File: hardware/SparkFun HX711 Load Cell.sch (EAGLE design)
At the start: 25 parts, among them Q1 MMBT4403, U1 HX711, U7 OSHW-LOGOS

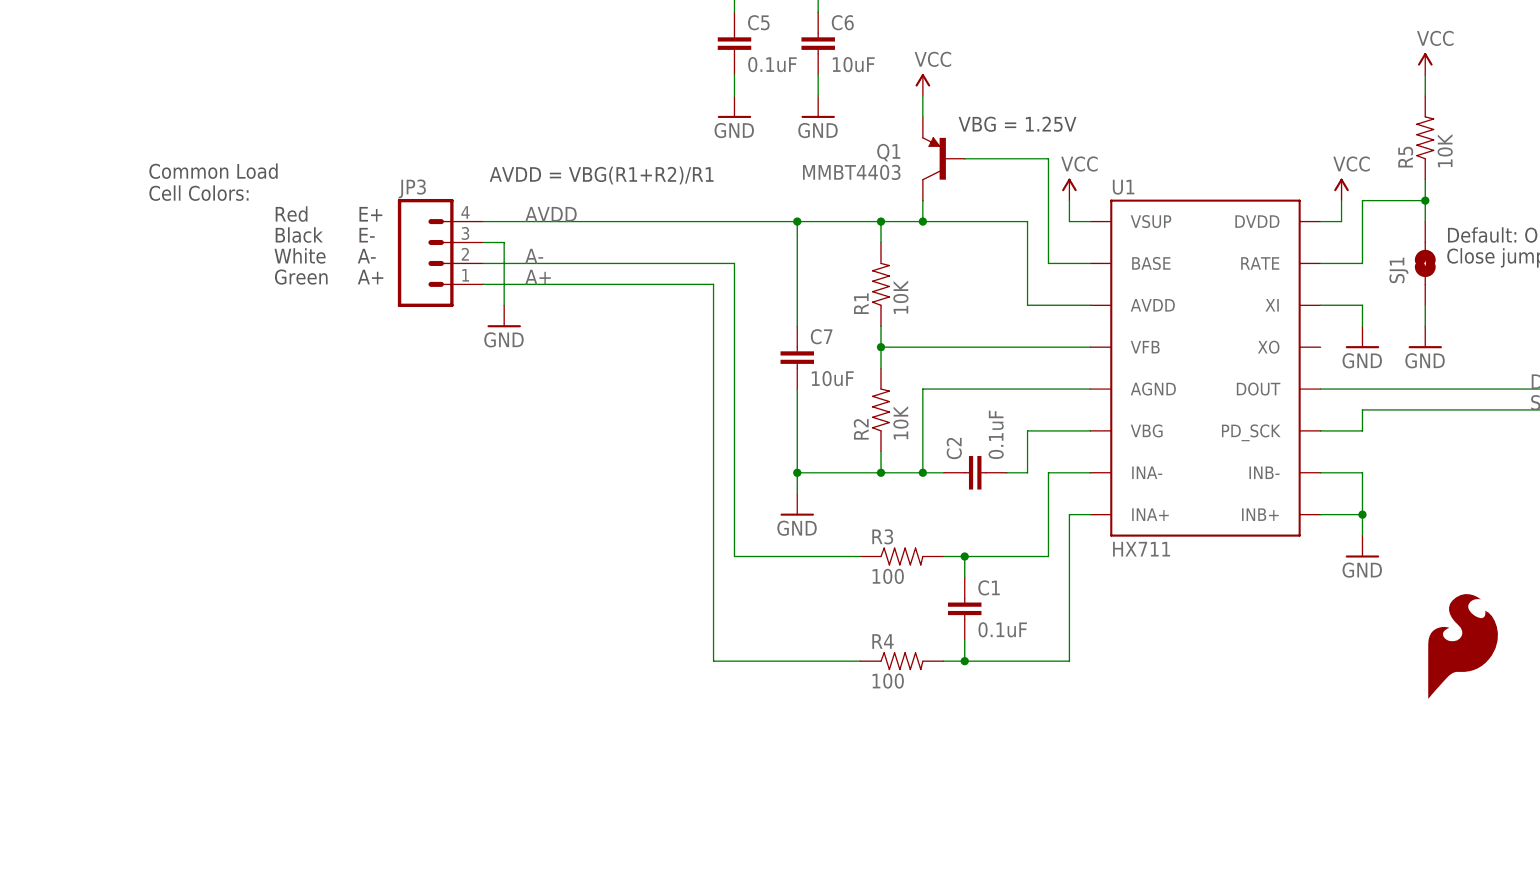
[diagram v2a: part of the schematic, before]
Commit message: Broke out channel B. Adjusted some traces.
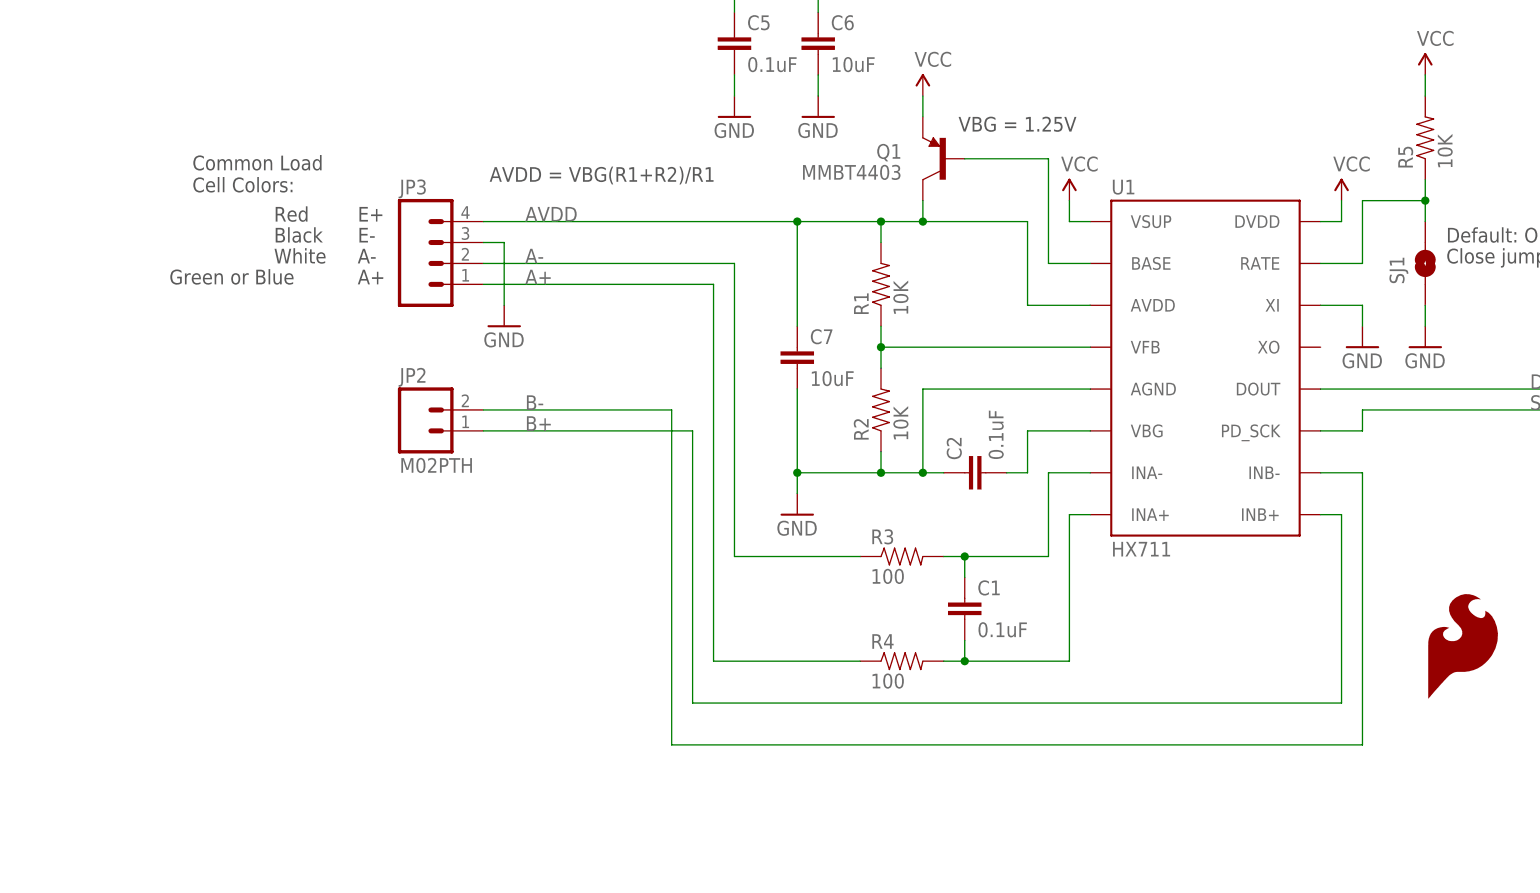
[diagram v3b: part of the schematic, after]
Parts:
- added JP2: M02PTH, SparkFun-Connectors:M02PTH
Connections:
- new net B+: JP2.1, U1.INB+
- new net B-: JP2.2, U1.INB-
- net GND: no longer U1.INB+, U1.INB-
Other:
- note added: "Green or Blue"
- note removed: "Green"
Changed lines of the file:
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@@
 <?xml version="1.0" encoding="utf-8"?>
 <!DOCTYPE eagle SYSTEM "eagle.dtd">
-<eagle version="6.5.0">
+<eagle version="7.1.0">
 <drawing>
 <settings>
@@
 <layer number="56" name="wert" color="7" fill="1" visible="no" active="no"/>
 <layer number="57" name="tCAD" color="7" fill="1" visible="no" active="no"/>
+<layer number="90" name="Modules" color="5" fill="1" visible="yes" active="yes"/>
 <layer number="91" name="Nets" color="2" fill="1" visible="yes" active="yes"/>
 <layer number="92" name="Busses" color="1" fill="1" visible="yes" active="yes"/>
@@
 <part name="GND5" library="SparkFun-Aesthetics" deviceset="GND" device=""/>
 <part name="JP3" library="SparkFun-Connectors" deviceset="M04" device="PTH"/>
-<part name="GND6" library="SparkFun-Aesthetics" deviceset="GND" device=""/>
 <part name="SUPPLY5" library="SparkFun-Aesthetics" deviceset="VCC" device=""/>
 <part name="R5" library="SparkFun-Resistors" deviceset="10KOHM1/10W1%(0603)" device="0603" value="10K"/>
@@
 <part name="FID1" library="SparkFun-Aesthetics" deviceset="FIDUCIAL" device="1X2"/>
 <part name="FID2" library="SparkFun-Aesthetics" deviceset="FIDUCIAL" device="1X2"/>
+<part name="JP2" library="SparkFun-Connectors" deviceset="M02" device="PTH"/>
 </parts>
 <sheets>
@@
 <text x="38.1" y="121.92" size="1.778" layer="97">Black</text>
 <text x="38.1" y="119.38" size="1.778" layer="97">White</text>
-<text x="38.1" y="116.84" size="1.778" layer="97">Green</text>
-<text x="22.86" y="127" size="1.778" layer="97">Common Load
+<text x="25.4" y="116.84" size="1.778" layer="97">Green or Blue</text>
+<text x="28.194" y="128.016" size="1.778" layer="97">Common Load
 Cell Colors:</text>
 <text x="172.72" y="10.16" size="1.778" layer="94">N. Seidle</text>
@@
 <instance part="GND5" gate="1" x="101.6" y="88.9"/>
 <instance part="JP3" gate="G$1" x="58.42" y="119.38"/>
-<instance part="GND6" gate="1" x="170.18" y="83.82"/>
 <instance part="SUPPLY5" gate="G$1" x="195.58" y="109.22"/>
 <instance part="R5" gate="G$1" x="177.8" y="134.62" rot="R90"/>
@@
 <instance part="FID1" gate="G$1" x="243.84" y="43.18"/>
 <instance part="FID2" gate="G$1" x="238.76" y="43.18"/>
+<instance part="JP2" gate="G$1" x="55.88" y="99.06"/>
 </instances>
 <busses>
@@
 <junction x="101.6" y="93.98"/>
 <pinref part="C2" gate="G$1" pin="1"/>
-</segment>
-<segment>
-<pinref part="U1" gate="U1" pin="INB-"/>
-<pinref part="GND6" gate="1" pin="GND"/>
-<wire x1="165.1" y1="93.98" x2="170.18" y2="93.98" width="0.1524" layer="91"/>
-<wire x1="170.18" y1="93.98" x2="170.18" y2="88.9" width="0.1524" layer="91"/>
-<pinref part="U1" gate="U1" pin="INB+"/>
-<wire x1="170.18" y1="88.9" x2="170.18" y2="86.36" width="0.1524" layer="91"/>
-<wire x1="165.1" y1="88.9" x2="170.18" y2="88.9" width="0.1524" layer="91"/>
-<junction x="170.18" y="88.9"/>
 </segment>
 <segment>
@@
 </segment>
 </net>
+<net name="B+" class="0">
+<segment>
+<pinref part="U1" gate="U1" pin="INB+"/>
+<wire x1="165.1" y1="88.9" x2="167.64" y2="88.9" width="0.1524" layer="91"/>
+<wire x1="167.64" y1="88.9" x2="167.64" y2="66.04" width="0.1524" layer="91"/>
+<wire x1="167.64" y1="66.04" x2="88.9" y2="66.04" width="0.1524" layer="91"/>
+<wire x1="88.9" y1="66.04" x2="88.9" y2="99.06" width="0.1524" layer="91"/>
+<pinref part="JP2" gate="G$1" pin="1"/>
+<wire x1="88.9" y1="99.06" x2="63.5" y2="99.06" width="0.1524" layer="91"/>
+<label x="68.58" y="99.06" size="1.778" layer="95"/>
+</segment>
+</net>
+<net name="B-" class="0">
+<segment>
+<pinref part="U1" gate="U1" pin="INB-"/>
+<wire x1="165.1" y1="93.98" x2="170.18" y2="93.98" width="0.1524" layer="91"/>
+<wire x1="170.18" y1="93.98" x2="170.18" y2="60.96" width="0.1524" layer="91"/>
+<wire x1="170.18" y1="60.96" x2="86.36" y2="60.96" width="0.1524" layer="91"/>
+<wire x1="86.36" y1="60.96" x2="86.36" y2="101.6" width="0.1524" layer="91"/>
+<pinref part="JP2" gate="G$1" pin="2"/>
+<wire x1="86.36" y1="101.6" x2="63.5" y2="101.6" width="0.1524" layer="91"/>
+<label x="68.58" y="101.6" size="1.778" layer="95"/>
+</segment>
+</net>

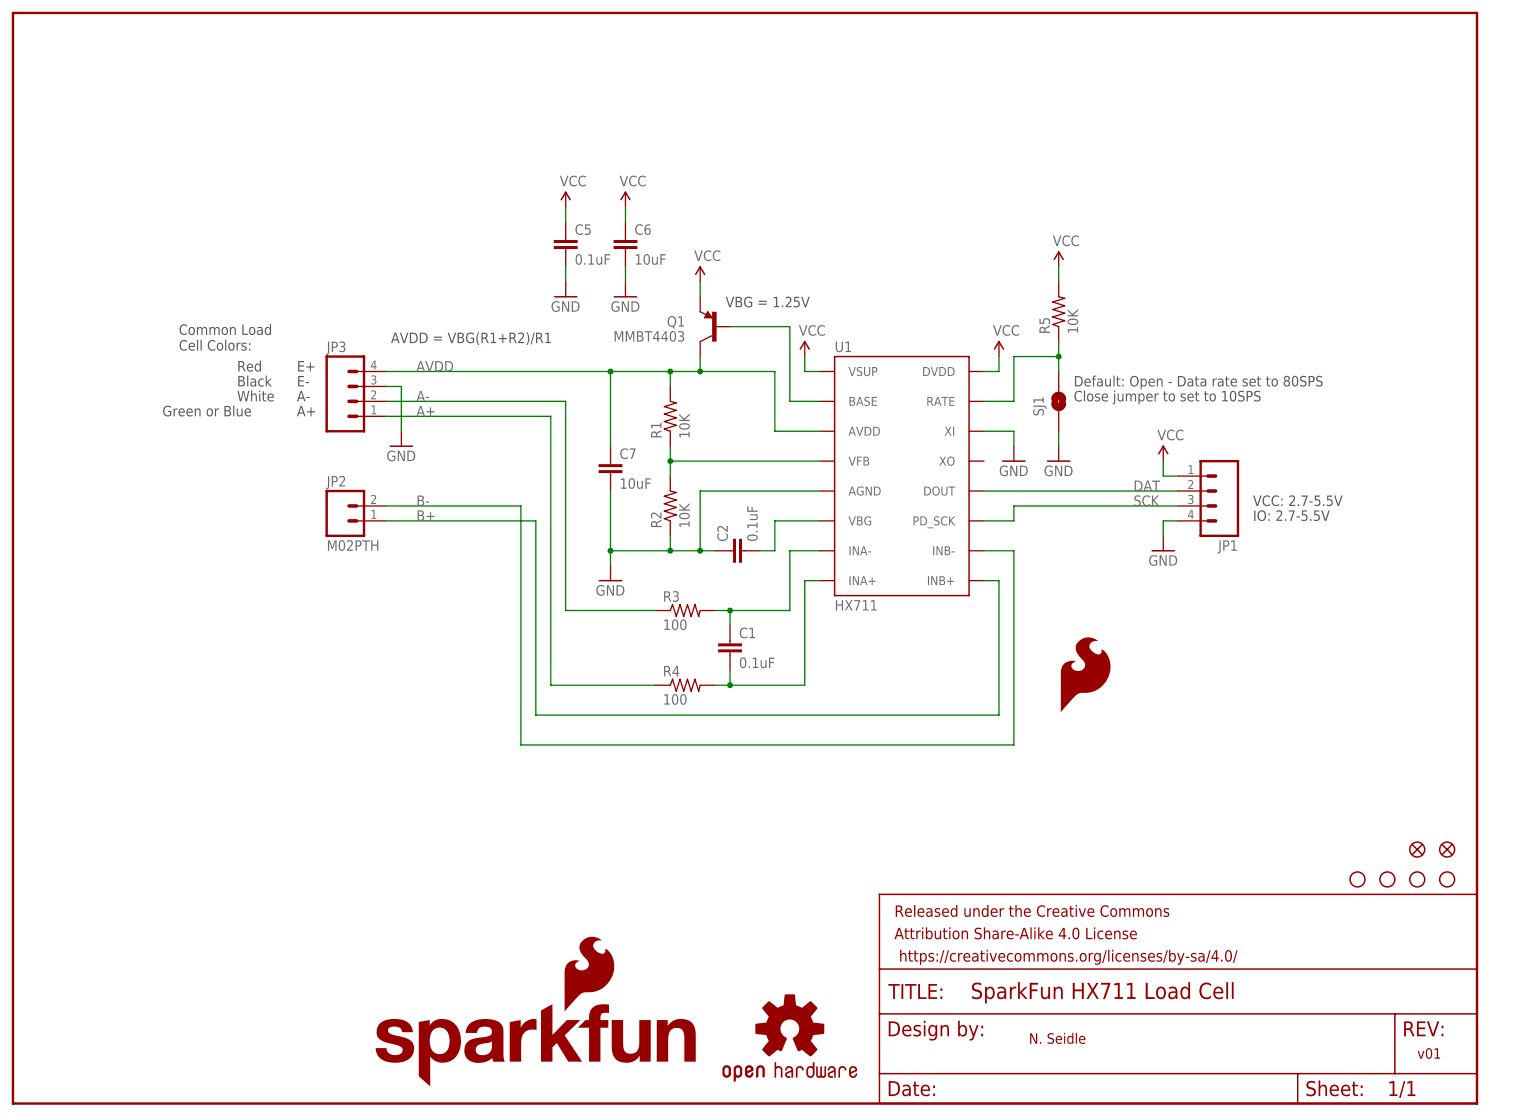
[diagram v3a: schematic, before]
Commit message: Silk label adjustment. Added cnt for shielding (yellow).
Some load cells have a 5th wire that is yellow that shields the four
wires. Added a ground connection for this 5th wire.
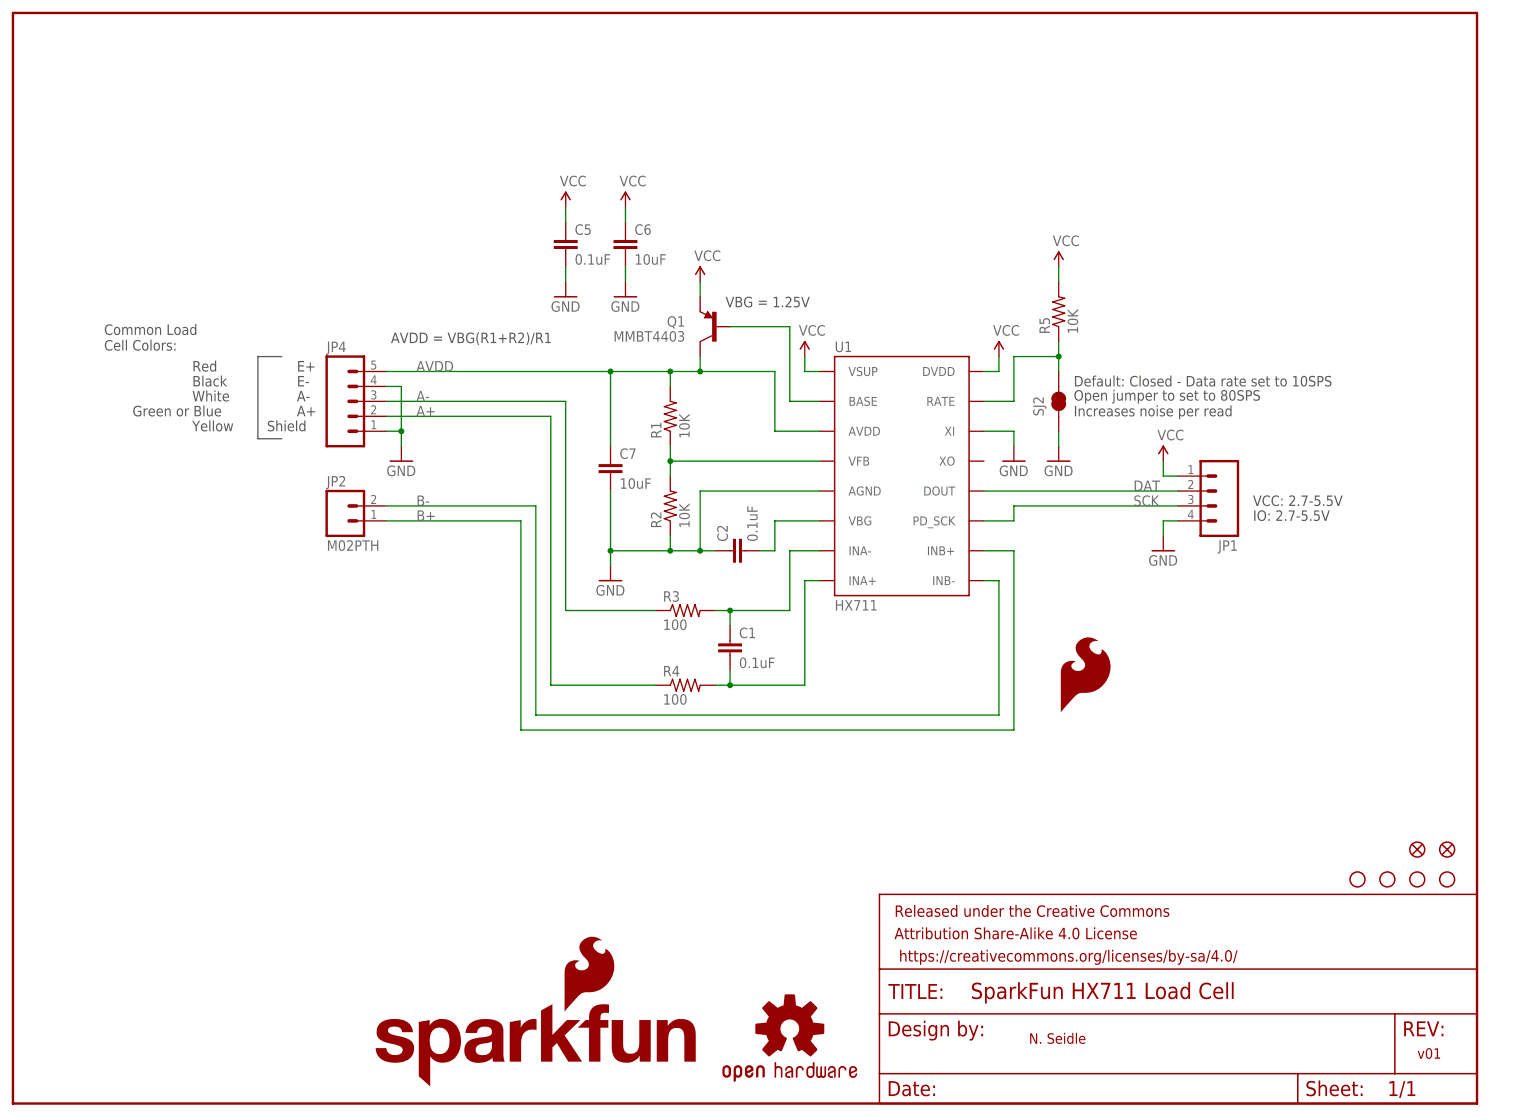
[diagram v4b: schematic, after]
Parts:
- removed JP3: (no value), SparkFun-Connectors:M04PTH
- removed SJ1: JUMPER-PAD-2-NOYES_SILK, SparkFun-Passives:JUMPER-PAD-2-NOYES_SILK
- added JP4: (no value), SparkFun-Connectors:M05PTH
- added SJ2: JUMPER-PAD-2-NC_BY_TRACE, SparkFun-Passives:JUMPER-PAD-2-NC_BY_TRACE
- R1, R2, R5: device SparkFun-Resistors:10KOHM1/10W1%(0603)0603 -> SparkFun-Resistors:10KOHM-1/10W-1%(0603)0603
- R3, R4: device SparkFun-Resistors:100OHM1/10W1%(0603) -> SparkFun-Resistors:100OHM-1/10W-1%(0603)
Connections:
- net A+: now also JP4.2; no longer JP3.1
- net A-: now also JP4.3; no longer JP3.2
- net AVDD: now also JP4.5; no longer JP3.4
- net GND: now also JP4.1, JP4.4, SJ2.1; no longer JP3.3, SJ1.1
- net N$1: now also SJ2.2; no longer SJ1.2
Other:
- note added: "Default: Closed - Data rate set to 10SPS"
- note added: "Open jumper to set to 80SPS Increases noise per read"
- note added: "Shield"
- note added: "Yellow"
- note removed: "Close jumper to set to 10SPS"
- note removed: "Default: Open - Data rate set to 80SPS"

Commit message: Change AVDD resistors to output closer to 5V
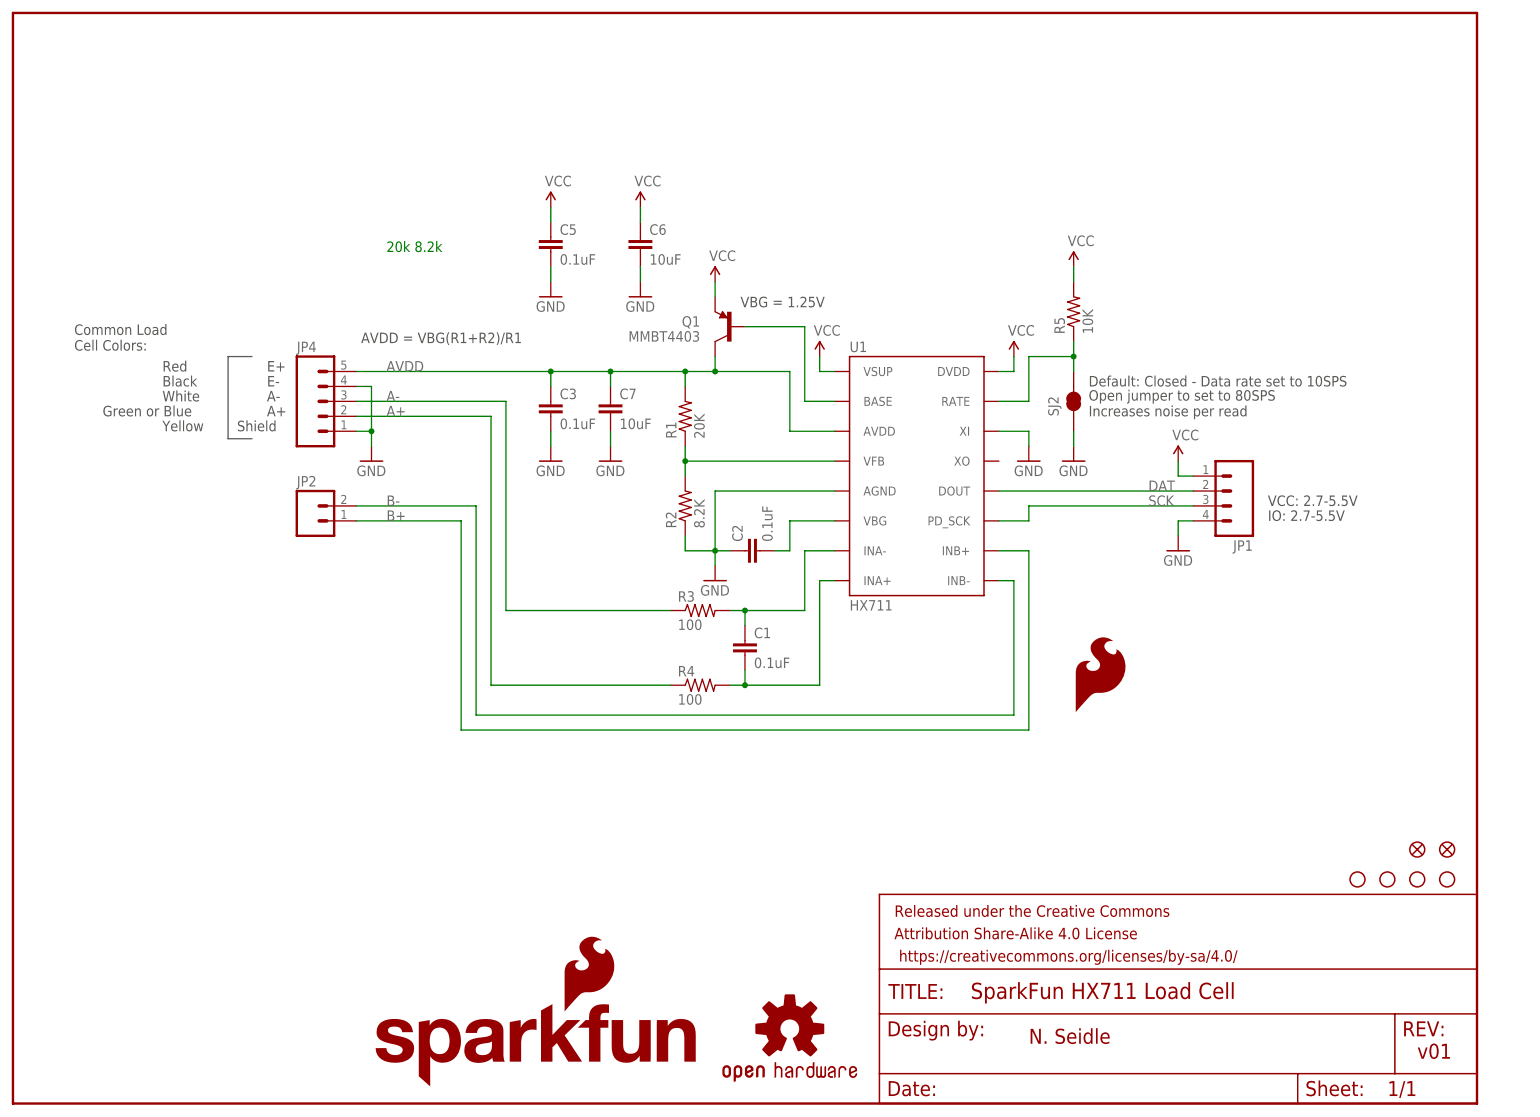
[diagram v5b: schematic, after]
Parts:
- added C3: 0.1uF, SparkFun-Capacitors:0.1UF-25V-5%(0603)
- R1: value 10K -> 20K; device SparkFun-Resistors:10KOHM-1/10W-1%(0603)0603 -> SparkFun-Resistors:20KOHM1/10W1%(0603)
- R2: value 10K -> 8.2K; device SparkFun-Resistors:10KOHM-1/10W-1%(0603)0603 -> SparkFun-Resistors:8.2KOHM-1/10W-5%(0603)
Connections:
- net AVDD: now also C3.1
- net GND: now also C3.2
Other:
- note added: "20k 8.2k"
- moved on the sheet: C1, C2, C5, C6, C7, JP1, JP2, JP4, Q1, R1, R2, R3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
